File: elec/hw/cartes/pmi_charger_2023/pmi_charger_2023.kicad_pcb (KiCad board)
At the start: 2 copper layers, 36.2 x 41 mm, 34 parts, among them J1 BTC-TC6S-23, SW1 MSS12C02LS-BB2.0, SW2 MSS12C02LS-BB2.0, U1 BQ25308RTER

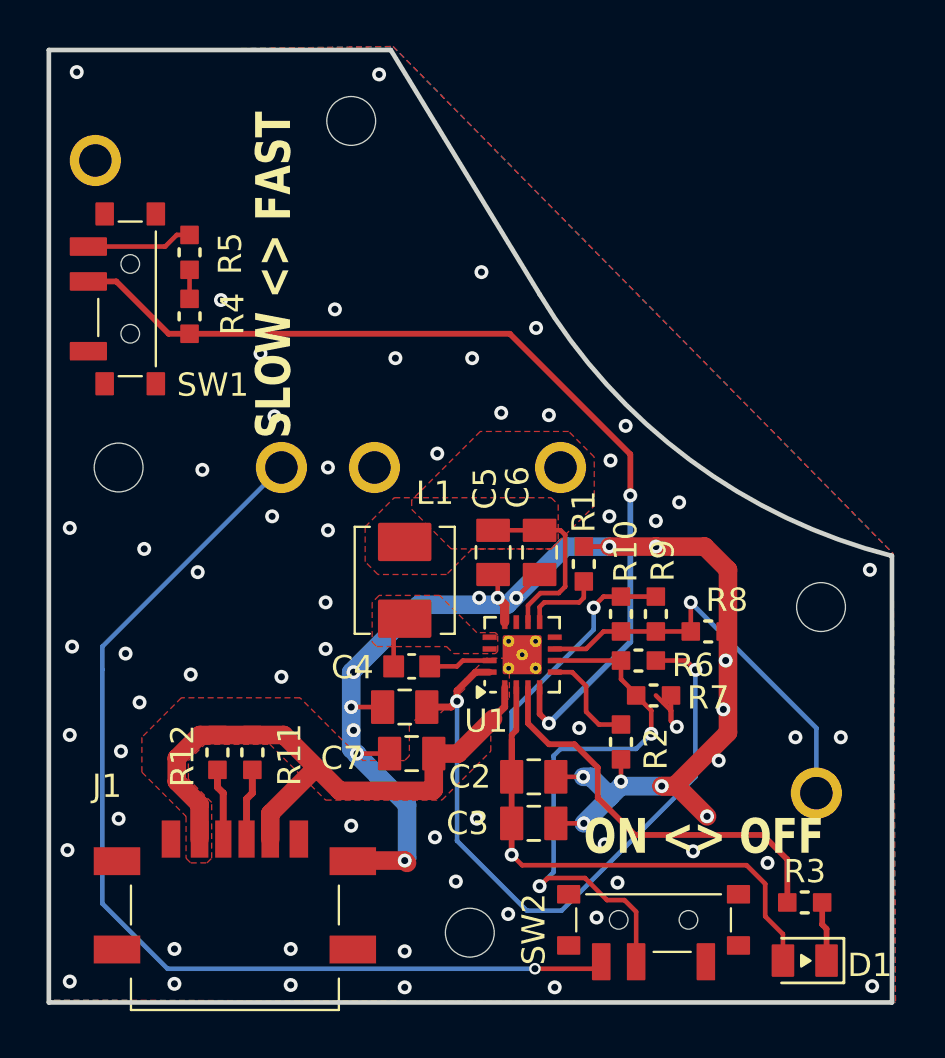
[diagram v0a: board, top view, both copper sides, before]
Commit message: fix:CC1/CC2 corrected, R6 connected to VBUS, R7 : set to unmounted
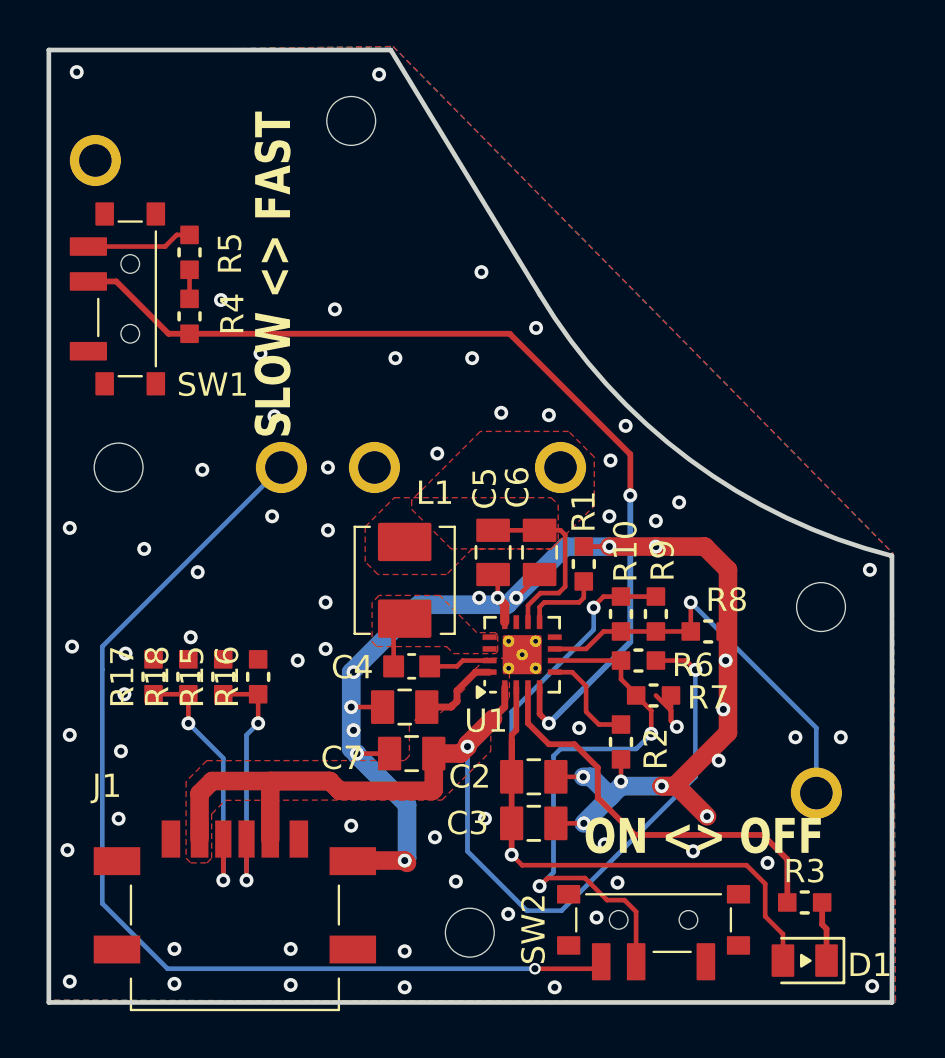
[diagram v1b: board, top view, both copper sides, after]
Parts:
- removed R11, R12: 10k 1%, cocotter_resistor:r0603_reflow
- added R15: 10k 1%, cocotter_resistor:r0603_reflow, F.Cu at (107.5, 86.0)
- added R16: 10k 1%, cocotter_resistor:r0603_reflow, F.Cu at (109.0, 86.0)
- added R17: 10k 1%, cocotter_resistor:r0603_reflow, F.Cu at (104.5, 86.0)
- added R18: 10k 1%, cocotter_resistor:r0603_reflow, F.Cu at (106.0, 86.0)
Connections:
- R6 pad 1: Net-(U1-PMID) -> VBUS
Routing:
- net Net-(U1-PMID): track 29.9 -> 3.58 mm, vias 2 -> 0
- net VBUS: track 26.5 -> 48.0 mm, vias 0 -> 2
- net Net-(J1-CC1): track 3.08 -> 11.9 mm, vias 0 -> 2
- net Net-(J1-CC2): track 3.08 -> 11.5 mm, vias 0 -> 2

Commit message: PAMI charger: fix silkscreen
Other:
- board text added: "LED status : OFF : charged ON : charging blink : fault"
